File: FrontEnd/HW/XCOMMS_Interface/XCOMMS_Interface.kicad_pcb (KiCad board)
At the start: 4 copper layers, 40 x 65 mm, 100 parts, among them J1 TFC-110-02-F-D-A-P-FR, J2 UART, J3 JTAG, J4 12V, U1 STM32L431KBUx, U10 MAX870EUK, U2 TPS56637, U3 TPS56637, U4 TPS56637, U5 TPS784, U6 MAX870EUK, U7 INA290, U8 AD5160, U9 MAX870EUK, Y1 TCXO_ECS

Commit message: XCOMMS Interface rebuild
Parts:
- removed C_TCXO1: 100nF, Capacitor_SMD:C_0603_1608Metric
- removed Designator10 (x2), Designator11, Designator6: Comment, D:_GoogleDrive_UPC_MEE_IR_Altium_Library_Altium_libraries_3CAT_Official_lib_3C4_OFFICIAL_LIB.PcbLib_PCB_ID
- removed Designator7: Comment, D:_GoogleDrive_UPC_MEE_IR_Altium_Library_Altium_libraries_3CAT_Official_lib_3C4_OFFICIAL_LIB.PcbLib_PCB_Rev
- removed Designator8: Comment, D:_GoogleDrive_UPC_MEE_IR_Altium_Library_Altium_libraries_3CAT_Official_lib_3C4_OFFICIAL_LIB.PcbLib_NANOSAT_LOGO
- removed Designator9: Comment, D:_GoogleDrive_UPC_MEE_IR_Altium_Library_Altium_libraries_3CAT_Official_lib_3C4_OFFICIAL_LIB.PcbLib_UPC_LOGO
- added Annotation1: Silkscreen_Annotation, GGS_Symbols:Bike, F.Cu at (130.5, 130.9)
- added Annotation2: Silkscreen_Annotation, GGS_Symbols:GGS, F.Cu at (145.0, 128.0)
- added Annotation3: Silkscreen_Annotation, GGS_Symbols:NSL, F.Cu at (151.7, 136.5)
- added Annotation4: Silkscreen_Annotation, GGS_Symbols:Prj, F.Cu at (135.0, 125.0)
- added Annotation5: Silkscreen_Annotation, GGS_Symbols:Rev, F.Cu at (135.0, 128.0)
- added Annotation6: Silkscreen_Annotation, GGS_Symbols:UPC, F.Cu at (137.0, 136.0)
- added C41: 20nF, Capacitor_SMD:C_0603_1608Metric, B.Cu at (162.9, 85.9)
- added D1: SZESD9X3.3ST5G, Diode_SMD:D_SOD-923, F.Cu at (155.9, 115.2)
- added D2: SZESD9X3.3ST5G, Diode_SMD:D_SOD-923, F.Cu at (155.0, 113.7)
- added D3: SZESD9X3.3ST5G, Diode_SMD:D_SOD-923, F.Cu at (155.9, 111.3)
- added D4: SZESD9X3.3ST5G, Diode_SMD:D_SOD-923, F.Cu at (156.2, 88.6)
- added D5: SZESD9X3.3ST5G, Diode_SMD:D_SOD-923, F.Cu at (156.2, 86.2)
- added R22: 10k, Resistor_SMD:R_0603_1608Metric, B.Cu at (162.9, 87.5)
- added R23: 10k, Resistor_SMD:R_0603_1608Metric, F.Cu at (155.7, 84.2)
- added R24: 10k, Resistor_SMD:R_0603_1608Metric, F.Cu at (153.2, 82.5)
- added R25: 22R, Resistor_SMD:R_0603_1608Metric, F.Cu at (157.9, 114.8)
- added R26: 22R, Resistor_SMD:R_0603_1608Metric, F.Cu at (157.9, 113.3)
- added R27: 22R, Resistor_SMD:R_0603_1608Metric, F.Cu at (157.9, 111.8)
- added R28: 22R, Resistor_SMD:R_0603_1608Metric, F.Cu at (158.5, 88.1)
- added R29: 22R, Resistor_SMD:R_0603_1608Metric, F.Cu at (158.5, 86.6)
- C1, C10, C11, C13, C14, C19, C20, C21, C22, C23, C24, C7, C8: footprint Capacitor_SMD:C_0805_2012Metric -> Capacitor_SMD:C_0603_1608Metric
- C5: value 1uF -> 100nF
- C6: value 100nF -> 20nF
- J2: value UART -> PicoBlade01x05; footprint Connector_Molex:Molex_PicoBlade_53261-0471_1x04-1MP_P1.25mm_Horizontal -> Connector_Molex:Molex_PicoBlade_53261-0571_1x05-1MP_P1.25mm_Horizontal
- J3: value JTAG -> PicoBlade01x05; footprint Connector_Molex:Molex_PicoBlade_53261-0471_1x04-1MP_P1.25mm_Horizontal -> Connector_Molex:Molex_PicoBlade_53261-0571_1x05-1MP_P1.25mm_Horizontal
- J4: value 12V -> PicoBlade01x02
- U1: value STM32L431KBUx -> STM32L051K8Tx; footprint Package_DFN_QFN:QFN-32-1EP_5x5mm_P0.5mm_EP3.45x3.45mm -> Package_QFP:LQFP-32_7x7mm_P0.8mm
- Y1: value TCXO_ECS -> ECS-160-8-36B-CKY-TR3; footprint GGS_Miscellaneous:TCXO_ECS -> Oscillator:Oscillator_SMD_ECS_2520MV-xxx-xx-4Pin_2.5x2.0mm
- moved J2 15.0 mm to (164.8, 114.5)
- moved C6 9.09 mm to (162.9, 80.9)
- moved Y1 8.78 mm to (163.0, 83.4)
- moved C2 8.32 mm to (162.1, 91.3), turned to -90 degrees
- moved C1 7.84 mm to (163.7, 91.3), turned to -90 degrees
- moved C3 6.28 mm to (157.7, 78.0)
- moved R1 3.47 mm to (155.7, 78.0)
- moved C4 3.42 mm to (147.5, 87.3), turned to 90 degrees
- moved C5 2.83 mm to (162.9, 89.0), turned to 0 degrees
- moved TP2 1.93 mm to (142.4, 107.2)
- moved J4 1.45 mm to (164.7, 125.9)
- moved J3 1.25 mm to (164.8, 86.8)
- moved U1 1.22 mm to (153.6, 85.2)
- moved TP4 0.49 mm to (133.6, 86.1)
- moved TP7 0.49 mm to (133.6, 99.8)
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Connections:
- net /Boot0 renamed /BOOT0
- net /CurrentSense renamed /Id_PA
- C5 pad 1: +3V3 -> /NRST
- C6 pad 1: +3V3 -> /RCC_IN
- J1 pad 01: +5V -> /Pout_PA
- J1 pad 02: +3V3 -> /Vd_PA
- J1 pad 03: /Vd_PA -> /Vg_PA3
- J1 pad 04: /Tx_PM -> +5V
- J1 pad 05: /LO_EN -> /Vg_PA2
- J1 pad 07: /T_CSB -> /Vg_PA1
- J1 pad 08: GND -> /T_CSB
- J1 pad 09: /Tx_CE -> GND
- J1 pad 10: GND -> /PLL_CE
- J1 pad 12: GND -> +3V3
- J1 pad 15: /SCK -> GND
- J1 pad 16: /Vg_PA3 -> /SCK
- J1 pad 17: /SDO -> GND
- J1 pad 18: /Vg_PA2 -> /SDO
- J1 pad 19: /SDI -> GND
- J1 pad 20: /Vg_PA1 -> /SDI
- J2 pad 1: /USART1_CTS -> +3V3
- J2 pad 2: /USART1_Rx -> GND
- J2 pad 3: /USART1_Tx -> Net-(J2-Pad3)
- J2 pad 4: /USART1_CK -> Net-(J2-Pad4)
- J3 pad 1: /JTDO -> +12V
- J3 pad 2: /JTDI -> Net-(J3-Pad2)
- J3 pad 3: /JTCK -> Net-(J3-Pad3)
- J3 pad 4: /JTMS -> GND
- J4 pad 1: GND -> +12V
- J4 pad 2: +12V -> GND
- U1 pad 10: /LO_EN -> unconnected-(U1-Pad10)
- U1 pad 19: /USART1_Tx -> unconnected-(U1-Pad19)
- U1 pad 2: unconnected-(U1-Pad2) -> /RCC_IN
- U1 pad 20: /USART1_Rx -> unconnected-(U1-Pad20)
- U1 pad 21: /USART1_CTS -> unconnected-(U1-Pad21)
- U1 pad 22: unconnected-(U1-Pad22) -> /T_CSB
- U1 pad 23: /JTMS -> /TMS/SWDIO
- U1 pad 24: /JTCK -> /SCK/SWCLK
- U1 pad 25: /JTDI -> unconnected-(U1-Pad25)
- U1 pad 26: /JTDO -> unconnected-(U1-Pad26)
- U1 pad 29: /R_CSB -> /I2C1_SCL
- U1 pad 3: unconnected-(U1-Pad3) -> /RCC_OUT
- U1 pad 30: /T_CSB -> /I2C1_SDA
- U1 pad 4: unconnected-(U1-Pad4) -> /NRST
- U1 pad 6: /mcu_OSC -> unconnected-(U1-Pad6)
- U1 pad 7: /Tx_PM -> /Pout_PA
- U1 pad 9: unconnected-(U1-Pad9) -> /R_CSB
- Y1 pad 1: +3V3 -> /RCC_IN
- Y1 pad 3: /mcu_OSC -> /RCC_OUT
- Y1 pad 4: +3V3 -> GND
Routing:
- net /Pout_PA: track 0.00 -> 79.0 mm, vias 0 -> 2
- net /TMS/SWDIO: track 0.00 -> 66.8 mm, vias 0 -> 2
- net /SCK/SWCLK: track 0.00 -> 60.6 mm, vias 0 -> 2
- net +12V: track 49.1 -> 109.4 mm, vias 0 -> 3
- net /Tx_PM: track 43.7 -> 0.00 mm, vias 2 -> 0
- net +3V3: track 123.0 -> 81.3 mm, vias 6 -> 5
- net /NRST: track 0.00 -> 40.8 mm, vias 0 -> 2
- net /LO_EN: track 34.2 -> 0.00 mm, vias 2 -> 0
- net /Tx_CE: track 38.3 -> 6.14 mm, vias 2 -> 1
- net +5V: track 49.6 -> 22.1 mm
- net /SCK: track 38.8 -> 54.8 mm, vias 2 -> 4
- net /USART1_Tx: track 15.1 -> 0.00 mm
- net /USART1_Rx: track 13.7 -> 0.00 mm
- net /Vd_PA: track 24.0 -> 36.9 mm
- net /SDI: track 34.5 -> 47.3 mm, vias 2 -> 4
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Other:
- board text added: "XCOMMS Interface"
- board text added: "v2"

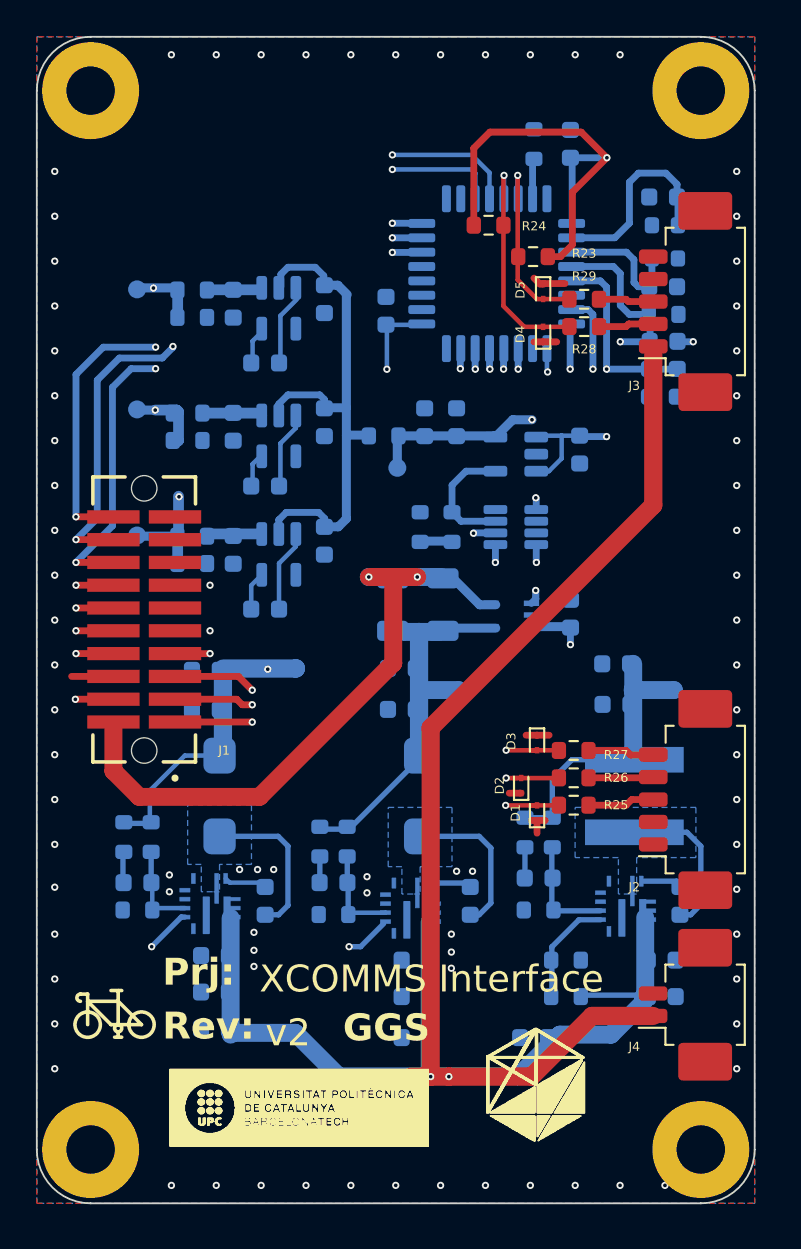
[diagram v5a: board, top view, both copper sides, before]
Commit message: xtal changed and routing
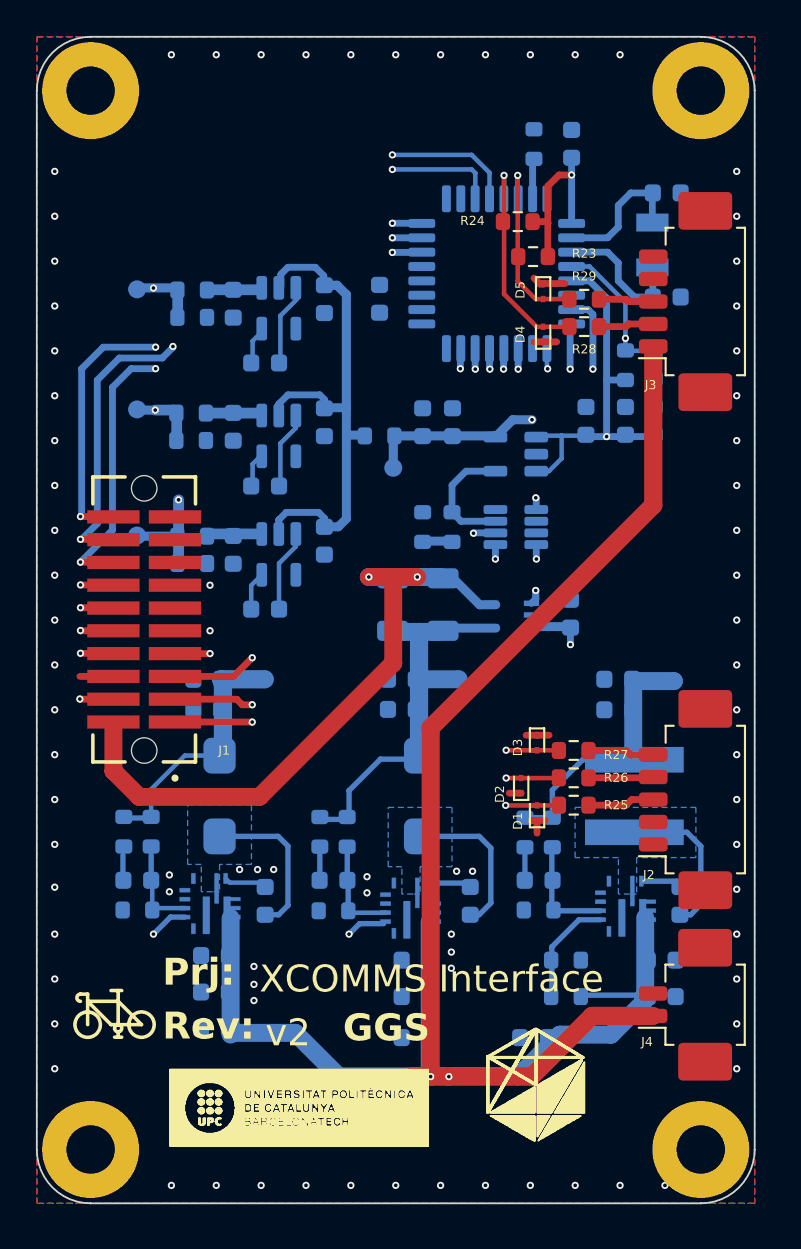
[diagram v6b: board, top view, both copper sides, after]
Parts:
- C41, C6: value 20nF -> 7pF
- Y1: value ECS-160-8-36B-CKY-TR3 -> ECS-.327-7-34QCS-TR; footprint Oscillator:Oscillator_SMD_ECS_2520MV-xxx-xx-4Pin_2.5x2.0mm -> Crystal:Crystal_SMD_3215-2Pin_3.2x1.5mm
- moved R22 3.54 mm to (160.8, 90.3), turned to 90 degrees
- moved C2 2.51 mm to (160.8, 93.4), turned to 90 degrees
- moved C1 2.48 mm to (162.4, 93.4), turned to 90 degrees
- moved TP2 1.85 mm to (140.7, 107.8)
- moved C30 1.64 mm to (158.6, 93.4), turned to 90 degrees
- moved R24 1.64 mm to (154.8, 82.3), turned to 180 degrees
- moved C5 1.43 mm to (162.4, 90.3), turned to -90 degrees
- moved C24 0.87 mm to (160.4, 107.8)
- moved C4 0.76 mm to (147.1, 86.6)
- moved Y1 0.72 mm to (162.3, 83.6), turned to 90 degrees
- moved C22 0.61 mm to (148.3, 107.8)
- moved C41 0.61 mm to (163.1, 86.5)
- moved TP1 0.60 mm to (151.5, 107.8)
- moved R3 0.54 mm to (145.3, 116.3)
- moved R4 0.54 mm to (143.8, 116.3)
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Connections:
- Y1 pad 2: GND -> /RCC_OUT
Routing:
- net +3V3: track 81.3 -> 63.5 mm, vias 5 -> 3
- net /Pout_PA: track 79.0 -> 74.5 mm
- net /RCC_IN: track 11.3 -> 7.92 mm
- net /5V_EN: track 43.0 -> 46.3 mm
- net /TMS/SWDIO: track 66.8 -> 63.6 mm
- net +5V: track 22.1 -> 19.4 mm, vias 3 -> 2
- net /SCK/SWCLK: track 60.6 -> 58.6 mm
- net /Vg_PA2: track 28.3 -> 26.4 mm
- net /SCK: track 54.8 -> 53.4 mm
- net GND: track 9.76 -> 8.47 mm, vias 83 -> 82
- net /6V_EN: track 38.7 -> 37.7 mm
- net /NRST: track 40.8 -> 40.0 mm
- net /SDI: track 47.3 -> 46.6 mm
- net /R_CSB: track 20.3 -> 19.6 mm
- net /SDO: track 37.4 -> 36.7 mm
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
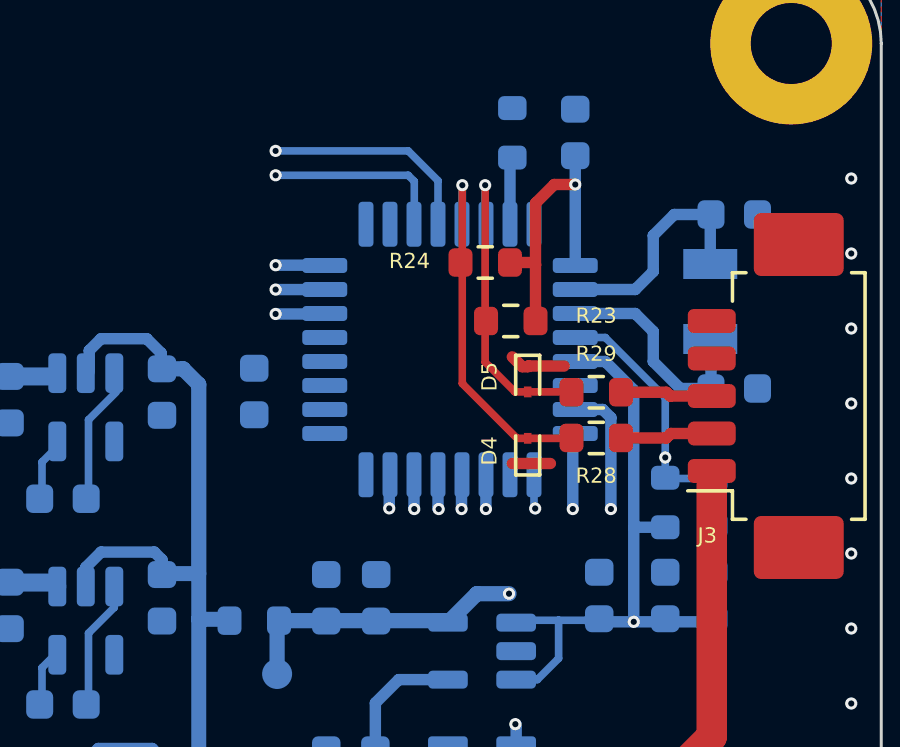
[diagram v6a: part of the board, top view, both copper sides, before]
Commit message: redundant MCU
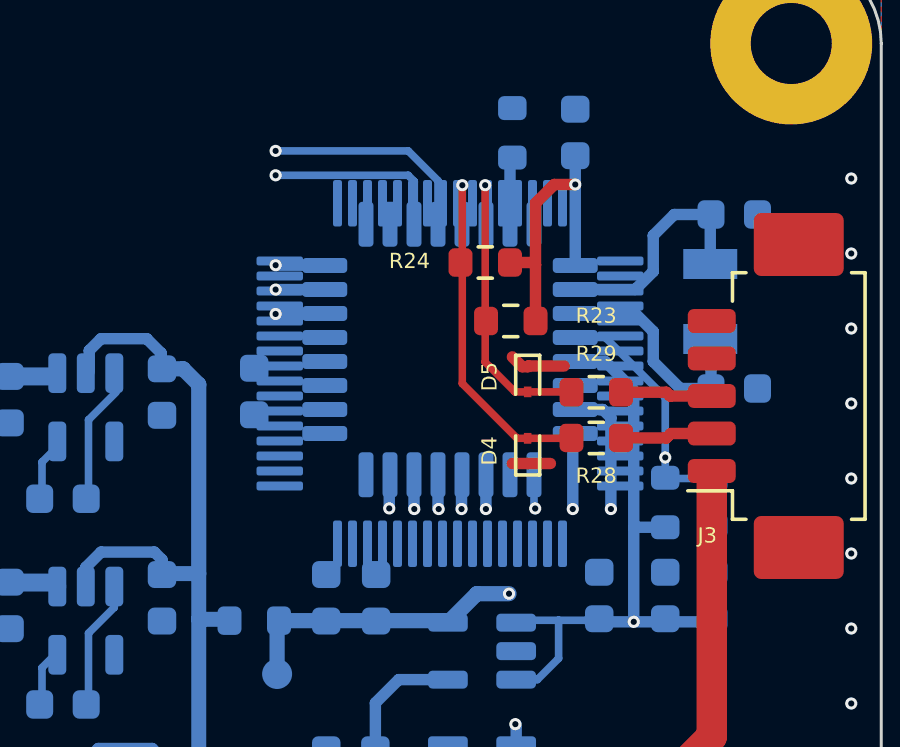
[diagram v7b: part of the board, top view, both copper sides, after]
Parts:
- added U11: STM32L053R8Tx, Package_QFP:LQFP-64_10x10mm_P0.5mm, B.Cu at (153.6, 86.0)
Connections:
- R23 pad 2: /I2C1_SDA -> /I2C1_SCL
- R24 pad 2: /I2C1_SCL -> /I2C1_SDA

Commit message: starting redundant mcu
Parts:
- U1: value STM32L051K8Tx -> STM32L431KBUx; footprint Package_QFP:LQFP-32_7x7mm_P0.8mm -> Package_DFN_QFN:QFN-32-1EP_5x5mm_P0.5mm_EP3.45x3.45mm
- moved C4 3.74 mm to (145.0, 83.5)
- moved C30 3.02 mm to (160.8, 95.5)
- moved C1 3.02 mm to (164.6, 95.5)
- moved C2 3.02 mm to (163.0, 95.5)
- moved C5 3.02 mm to (164.6, 92.4)
- moved R22 3.02 mm to (163.0, 92.4)
- moved C31 3.01 mm to (152.3, 96.3), turned to -90 degrees
- moved C32 3.01 mm to (150.6, 96.3), turned to -90 degrees
- moved C33 2.90 mm to (143.8, 89.5)
- moved TP4 2.90 mm to (133.4, 89.0)
- moved C29 2.90 mm to (138.7, 89.8)
- moved C34 2.90 mm to (140.5, 93.1)
- moved R13 2.90 mm to (136.4, 89.0)
- moved R15 2.90 mm to (136.4, 90.5)
- moved U6 2.90 mm to (141.3, 90.0)
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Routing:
- net /Pout_PA: track 74.5 -> 4.31 mm, vias 2 -> 0
- net /TMS/SWDIO: track 63.6 -> 3.27 mm, vias 2 -> 1
- net /SCK/SWCLK: track 58.6 -> 3.24 mm, vias 2 -> 1
- net /SCK: track 53.4 -> 2.60 mm, vias 4 -> 1
- net /5V_EN: track 46.3 -> 2.15 mm, vias 2 -> 1
- net /SDI: track 46.6 -> 2.64 mm, vias 4 -> 1
- net /PLL_CSB: track 47.0 -> 3.15 mm, vias 2 -> 1
- net /T_CSB: track 40.9 -> 1.84 mm, vias 2 -> 0
- net /6V_EN: track 37.7 -> 2.17 mm, vias 2 -> 1
- net /SDO: track 36.7 -> 1.84 mm, vias 3 -> 0
- net /NRST: track 40.0 -> 7.73 mm
- net +3V3: track 63.5 -> 35.8 mm, vias 3 -> 1
- net /Vg_PA1: track 31.2 -> 5.79 mm, vias 2 -> 1
- net /Vg_PA2: track 26.4 -> 8.31 mm, vias 2 -> 0
- net /R_CSB: track 19.6 -> 2.32 mm, vias 2 -> 1
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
